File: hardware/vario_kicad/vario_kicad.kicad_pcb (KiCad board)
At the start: 4 copper layers, 70 x 50 mm, 94 parts, among them Q1 NMOS, Q2 PMOS, U2 BME280, U3 W25Q128JVS, U4 USB C connector, U5 STM32L072CBTx, Y1 Crystal, Y2 Crystal_GND24

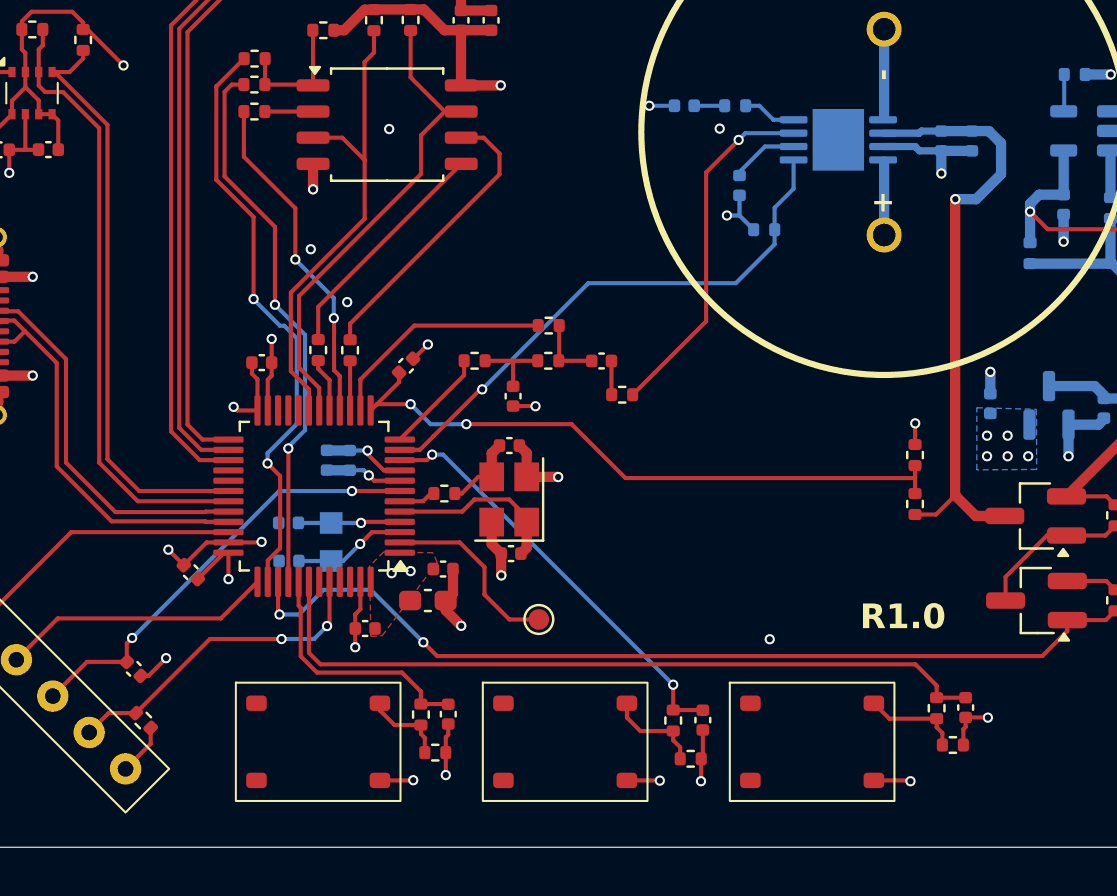
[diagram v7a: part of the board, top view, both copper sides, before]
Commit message: finished layout variant 2
- LSE on top
- increased clearance of copper pours
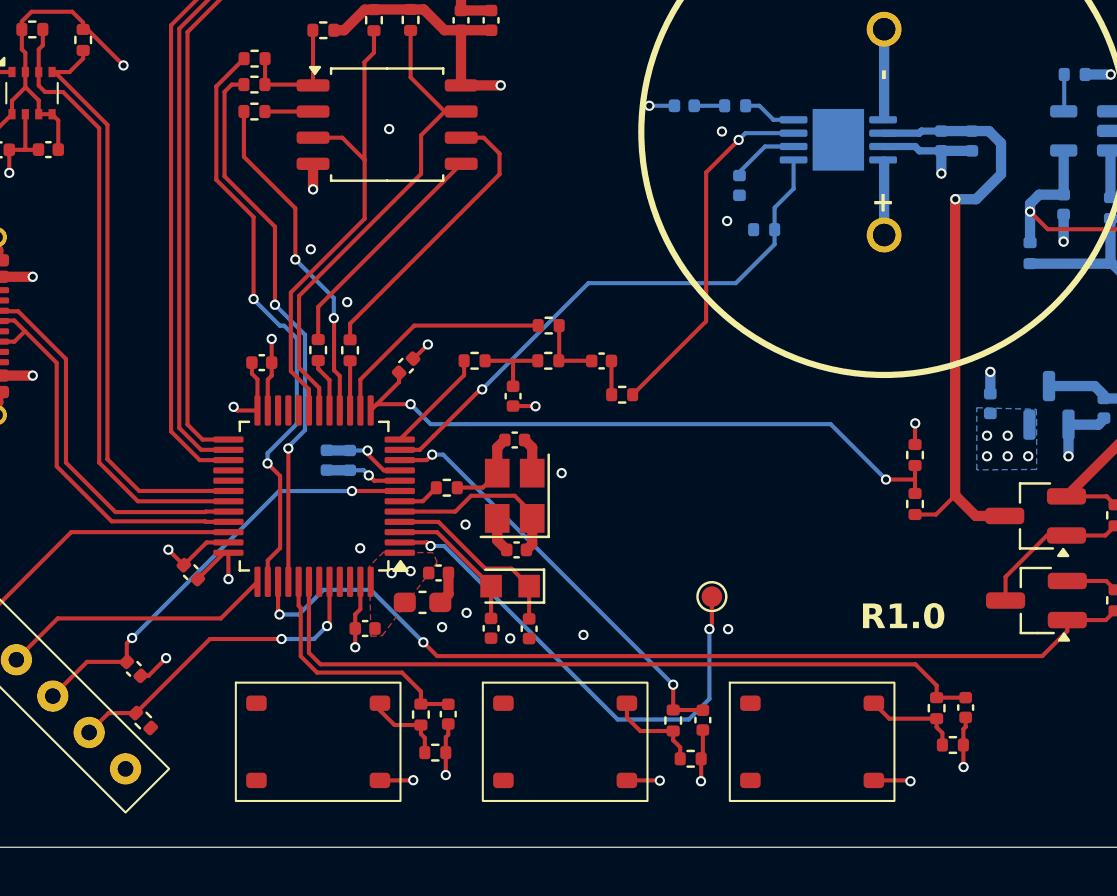
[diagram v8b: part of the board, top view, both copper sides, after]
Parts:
- C26, C27, Y1: moved to F.Cu
- moved C27 12.8 mm to (133.2, 139.4), turned to -90 degrees
- moved C26 10.4 mm to (131.4, 139.4), turned to -90 degrees
- moved Y1 8.96 mm to (132.3, 137.3), turned to 180 degrees
- moved TP4 8.48 mm to (142.1, 137.8)
- moved C20 0.37 mm to (132.6, 130.2)
- moved Y2 0.32 mm to (132.6, 132.9)
- moved C13 0.32 mm to (132.6, 135.6)
- moved R30 0.30 mm to (129.2, 132.5)
- moved C24 0.29 mm to (128.8, 136.7)
- moved C4 0.28 mm to (128.1, 138.1)
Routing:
- net /mcu/RTC_CALIB: track 9.09 -> 24.0 mm, vias 0 -> 2
- net GND: track 85.4 -> 74.6 mm, vias 45 -> 48
- net /mcu/OSC32_OUT: track 4.94 -> 9.17 mm, vias 1 -> 0
- net /mcu/OSC32_IN: track 5.48 -> 7.09 mm, vias 1 -> 0
